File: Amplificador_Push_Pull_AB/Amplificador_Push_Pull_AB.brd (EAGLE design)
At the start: 99 x 49.8 mm, 53 parts, among them IC1 LM741P, IC3 788TV, P2 10k, Q1 BC547, Q10 TIP42C, Q2 BC547, Q4 BC547, Q7 BC547, Q8 BC547, T2 2SC1307

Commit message: Wrong positioned jumper reallocated.
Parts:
- moved IC1 0.63 mm to (61.6, 11.4)
- moved RLEFT 0.63 mm to (77.5, 7.62)
- moved RRIGHT 0.63 mm to (74.9, 7.62)
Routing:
- net GND: track 359.7 -> 388.4 mm
- net N$26: track 27.8 -> 24.4 mm
- net N$27: track 63.3 -> 60.9 mm
- net -18V: track 172.3 -> 171.1 mm
- net VIN: track 7.25 -> 6.50 mm
- net N$12: track 10.4 -> 9.79 mm
- net N$14: track 17.2 -> 16.6 mm

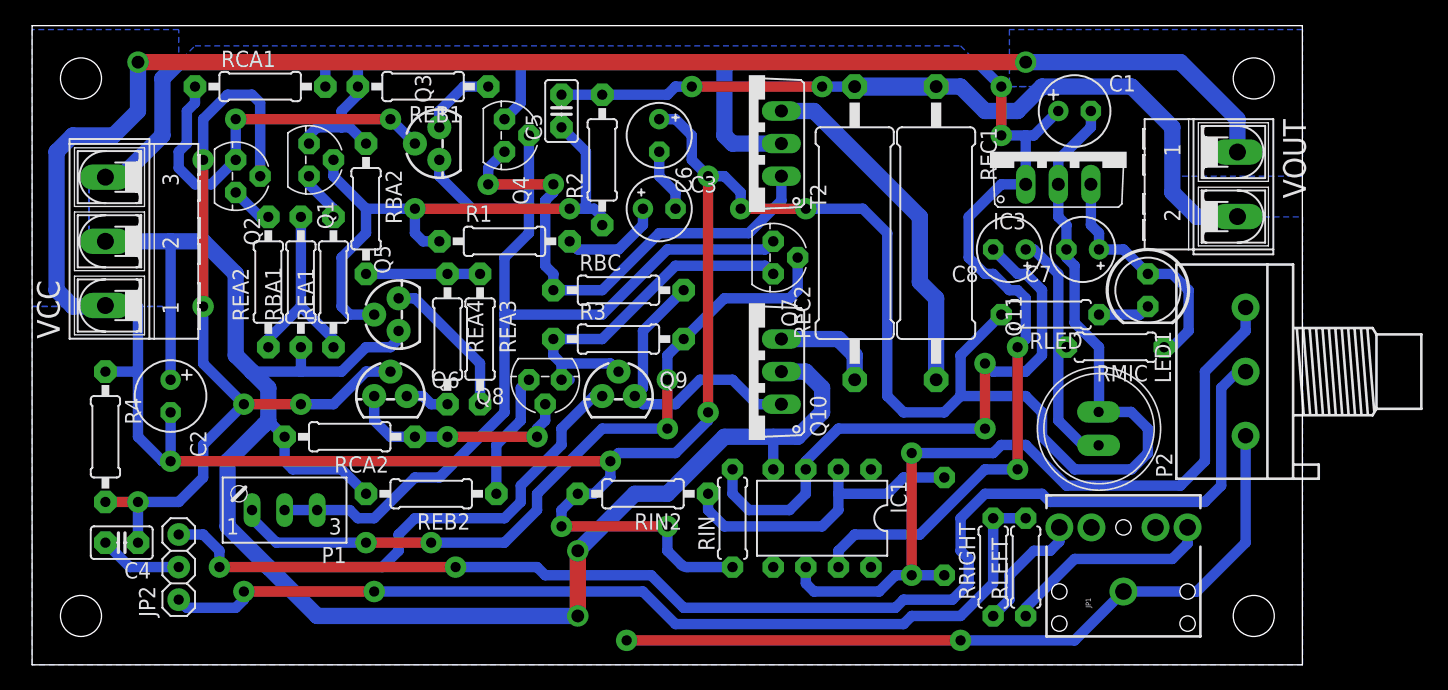
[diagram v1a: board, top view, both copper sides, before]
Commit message: Pads and vias increased outer diameter.
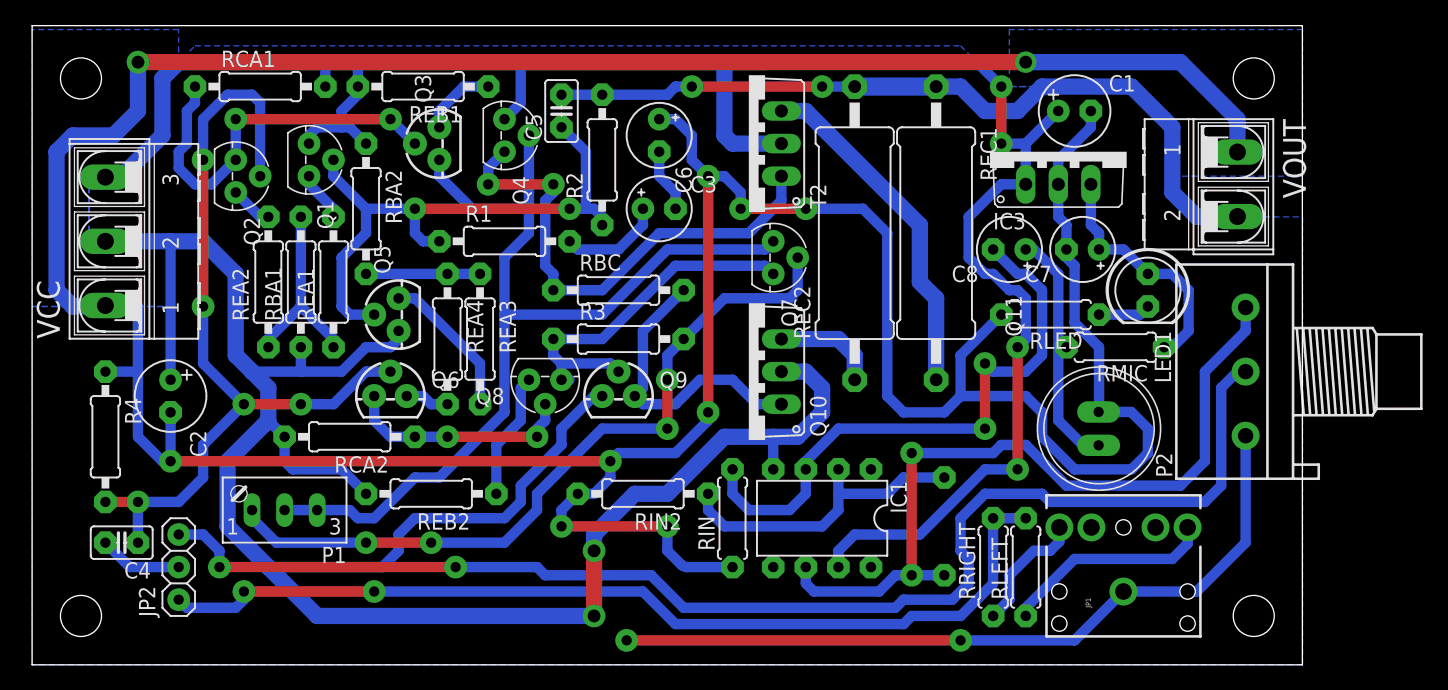
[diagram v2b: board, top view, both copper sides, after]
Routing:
- net -18V: track 171.1 -> 171.9 mm

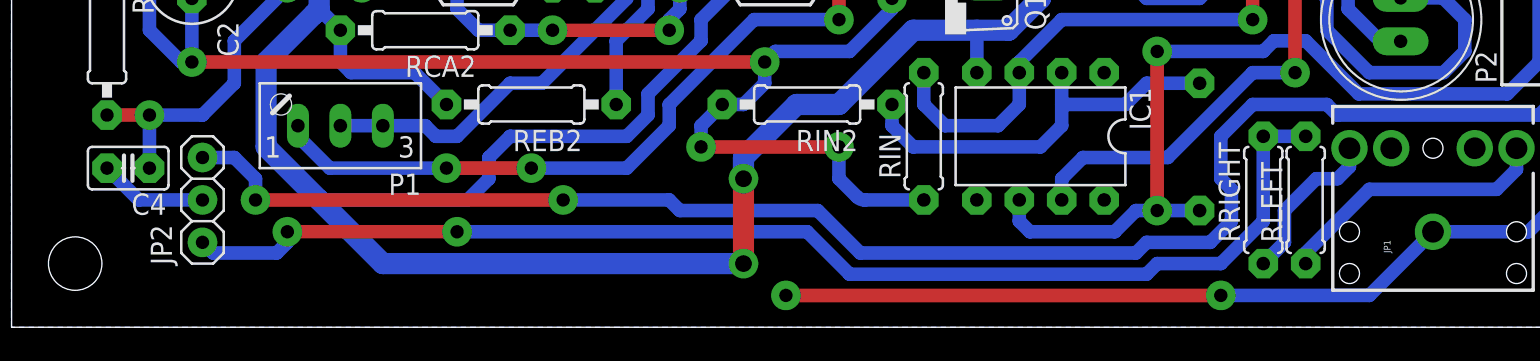
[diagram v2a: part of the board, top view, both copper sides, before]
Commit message: Double connection with jumper and resistor in one pad solved. Printable file genererated. Ready!!!
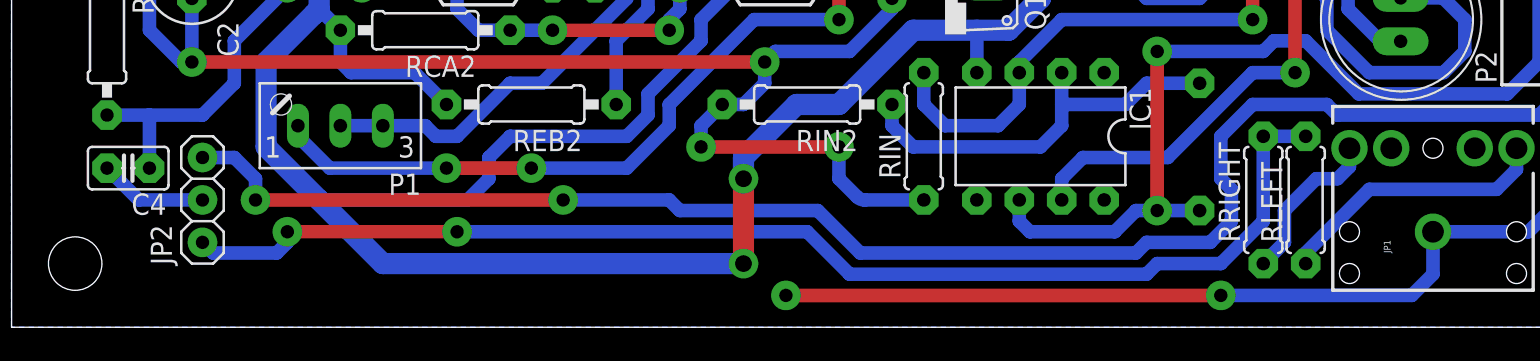
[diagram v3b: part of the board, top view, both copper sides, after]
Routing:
- net GND: track 388.4 -> 389.9 mm
- net HEHEAH: vias 5 -> 4
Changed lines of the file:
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@@
 <layer number="220" name="220bmp" color="21" fill="1" visible="no" active="no"/>
 <layer number="221" name="221bmp" color="22" fill="1" visible="no" active="no"/>
-<layer number="222" name="222bmp" color="23" fill="1" visible="no" active="no"/>
 <layer number="223" name="223bmp" color="24" fill="1" visible="no" active="no"/>
 <layer number="224" name="224bmp" color="25" fill="1" visible="no" active="no"/>
@@
 <wire x1="94.615" y1="9.525" x2="90.805" y2="5.715" width="0.8128" layer="16"/>
 <wire x1="90.805" y1="5.715" x2="85.09" y2="5.715" width="0.8128" layer="16"/>
-<wire x1="85.09" y1="5.715" x2="81.28" y2="1.905" width="0.8128" layer="16"/>
-<wire x1="81.28" y1="1.905" x2="72.39" y2="1.905" width="0.8128" layer="16"/>
+<wire x1="83.82" y1="1.905" x2="72.39" y2="1.905" width="0.8128" layer="16"/>
 <via x="72.39" y="1.905" extent="1-16" drill="0.8" diameter="1.778" shape="octagon"/>
 <wire x1="72.39" y1="1.905" x2="46.355" y2="1.905" width="0.8128" layer="1"/>
@@
 <wire x1="42.545" y1="13.335" x2="41.275" y2="12.065" width="0.8128" layer="16"/>
 <wire x1="41.275" y1="12.065" x2="41.275" y2="10.795" width="0.8128" layer="16"/>
+<wire x1="83.82" y1="1.905" x2="85.09" y2="3.175" width="0.8128" layer="16"/>
+<wire x1="85.09" y1="3.175" x2="85.09" y2="5.715" width="0.8128" layer="16"/>
 </signal>
 <signal name="N$13">
@@
 <via x="13.335" y="27.94" extent="1-16" drill="0.8" diameter="1.778" shape="octagon"/>
 <wire x1="23.495" y1="20.32" x2="26.035" y2="22.86" width="0.8128" layer="16"/>
-<wire x1="5.715" y1="12.7" x2="8.255" y2="12.7" width="0.8128" layer="1"/>
-<via x="8.255" y="12.7" extent="1-16" drill="0.8" diameter="1.778" shape="octagon"/>
 <wire x1="26.035" y1="22.86" x2="27.94" y2="22.86" width="0.8128" layer="16"/>
 <wire x1="23.495" y1="20.32" x2="20.955" y2="20.32" width="0.8128" layer="16"/>
@@
 <wire x1="15.24" y1="44.45" x2="13.335" y2="42.545" width="0.8128" layer="16"/>
 <wire x1="13.335" y1="42.545" x2="13.335" y2="39.37" width="0.8128" layer="16"/>
+<wire x1="5.715" y1="12.7" x2="8.255" y2="12.7" width="0.8128" layer="16"/>
 </signal>
 <signal name="N$18">

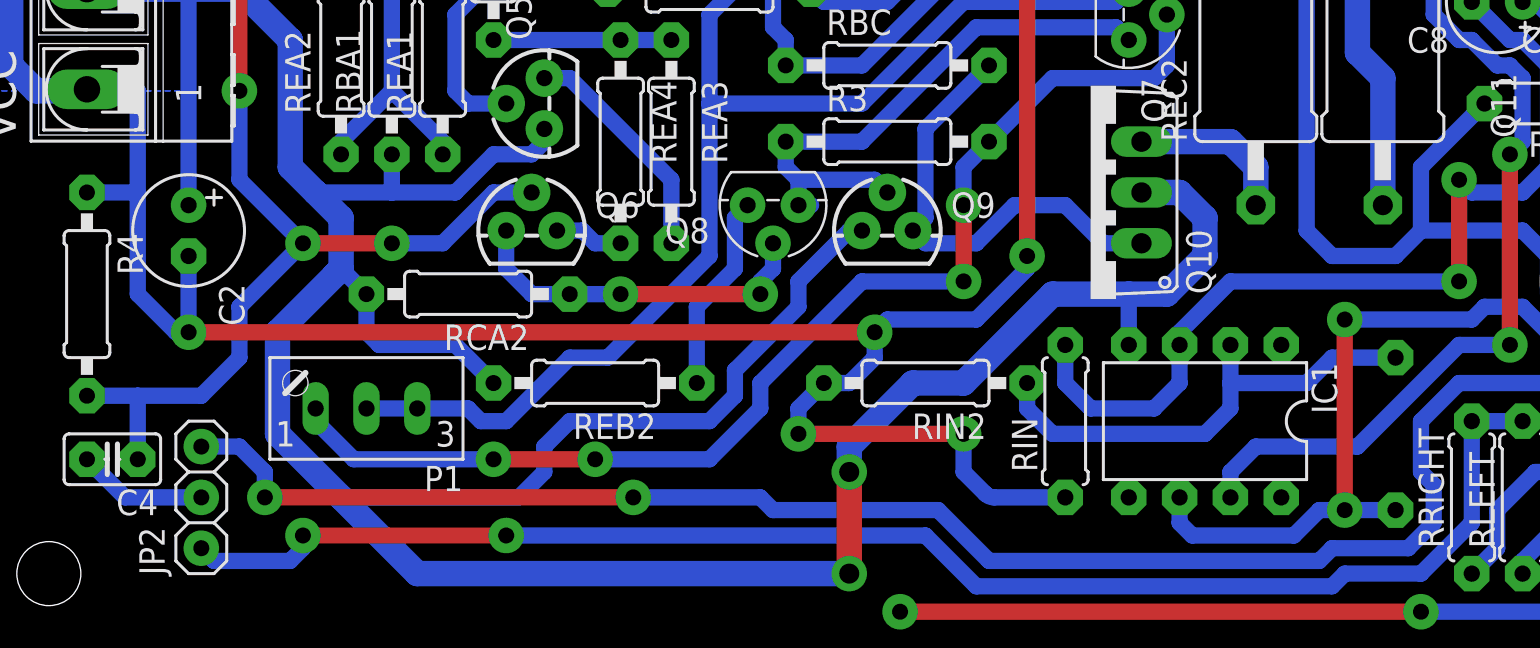
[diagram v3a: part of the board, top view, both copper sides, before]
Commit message: Inversed polarity capactitor problem solved. Simulation files added. PCB assembled and worked good! Next time: Limit the outputs's maximum voltage of the op. amp. through a smaller gain or decrease the potentiometer range; Also, swap the pin header used in channel selection for HH key bought.
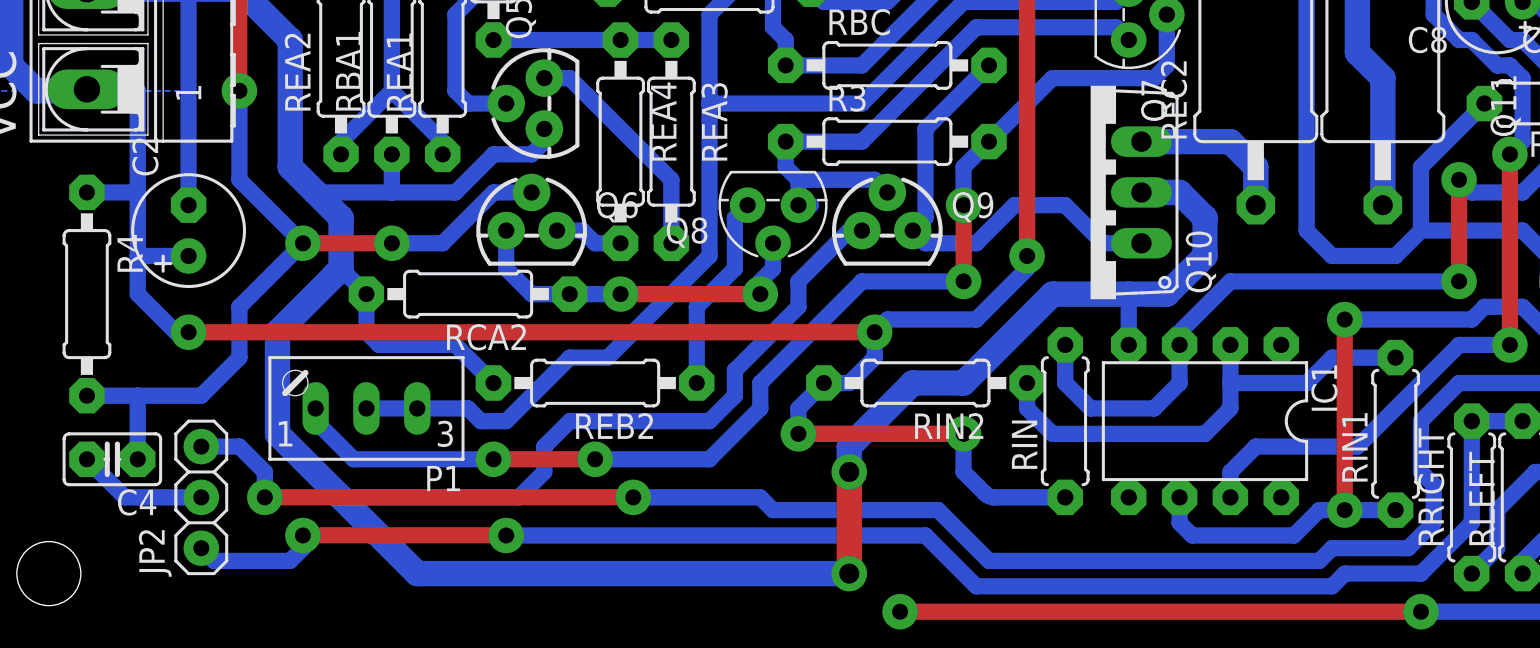
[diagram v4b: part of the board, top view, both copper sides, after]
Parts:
- C7, C8: value 0.1uF -> 0.68uF
- P2: value 10k -> 100k
- RIN1: value 100k -> 22k
- turned C2 to 90 degrees
- flipped RIN1 to the top
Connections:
- net -18V: now also C2.-; no longer C2.+
- net GND: now also C2.+; no longer C2.-
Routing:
- net GND: track 389.9 -> 388.6 mm
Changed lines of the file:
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@@
 <elements>
 <element name="C1" library="rcl" package="E2,5-6" value="100uF" x="81.28" y="43.18"/>
-<element name="C2" library="rcl" package="E2,5-6" value="100uF" x="10.795" y="20.955" rot="R270"/>
+<element name="C2" library="rcl" package="E2,5-6" value="100uF" x="10.795" y="20.955" rot="R90"/>
 <element name="C3" library="rcl" package="E2,5-5" value="10uF" x="48.895" y="35.56"/>
 <element name="Q1" library="transistor" package="TO92" value="BC547" x="21.59" y="39.37" rot="R270"/>
@@
 <element name="Q11" library="adafruit" package="9.7ELECTRET" value="" x="83.185" y="18.415" rot="R270"/>
 <element name="C6" library="rcl" package="E2,5-5" value="10uF" x="48.895" y="41.275" rot="R270"/>
-<element name="C7" library="rcl" package="E2,5-5" value="0.1uF" x="81.915" y="32.385" rot="R180"/>
-<element name="C8" library="rcl" package="E2,5-5" value="0.1uF" x="76.2" y="32.385" rot="R180"/>
+<element name="C7" library="rcl" package="E2,5-5" value="0.68uF" x="81.915" y="32.385" rot="R180"/>
+<element name="C8" library="rcl" package="E2,5-5" value="0.68uF" x="76.2" y="32.385" rot="R180"/>
 <element name="RIN" library="rcl" package="0207/7" value="100k" x="54.61" y="11.43" rot="R90"/>
-<element name="RIN1" library="rcl" package="0207/7" value="100k" x="71.12" y="10.795" rot="MR90"/>
+<element name="RIN1" library="rcl" package="0207/7" value="22k" x="71.12" y="10.795" rot="R90"/>
 <element name="RIN2" library="rcl" package="0207/10" value="10k" x="47.625" y="13.335" rot="R180"/>
-<element name="P2" library="pot" package="3RP/1610N" value="10k" x="94.615" y="22.86" rot="R90"/>
+<element name="P2" library="pot" package="3RP/1610N" value="100k" x="94.615" y="22.86" rot="R90"/>
 <element name="JP2" library="pinhead" package="1X03" value="" x="11.43" y="7.62" rot="R90"/>
 <element name="RLEFT" library="rcl" package="0207/7" value="10k" x="77.47" y="7.62" rot="R90"/>
@@
 <contactref element="R4" pad="1"/>
 <contactref element="C1" pad="-"/>
-<contactref element="C2" pad="-"/>
 <contactref element="VOUT" pad="1"/>
 <contactref element="VCC" pad="1"/>
@@
 <wire x1="5.07773125" y1="27.975521875" x2="5.1181" y2="27.9781" width="1.27" layer="16"/>
 <wire x1="5.1181" y1="27.9781" x2="5.715" y2="28.0162" width="1.27" layer="16"/>
-<wire x1="10.795" y1="19.685" x2="10.795" y2="15.875" width="0.8128" layer="16"/>
 <wire x1="5.715" y1="22.86" x2="8.255" y2="22.86" width="0.8128" layer="16"/>
 <via x="41.275" y="10.795" extent="1-16" drill="0.8" diameter="1.778" shape="octagon"/>
@@
 <wire x1="67.945" y1="19.685" x2="66.675" y2="20.955" width="0.8128" layer="16"/>
 <wire x1="66.675" y1="20.955" x2="66.675" y2="33.655" width="0.8128" layer="16"/>
-<wire x1="8.255" y1="17.78" x2="8.255" y2="22.86" width="0.8128" layer="16"/>
+<wire x1="8.255" y1="17.78" x2="8.255" y2="19.685" width="0.8128" layer="16"/>
+<wire x1="8.255" y1="19.685" x2="8.255" y2="22.86" width="0.8128" layer="16"/>
 <wire x1="8.255" y1="22.86" x2="8.255" y2="27.94" width="0.8128" layer="16"/>
 <wire x1="45.085" y1="14.605" x2="43.815" y2="13.335" width="0.8128" layer="16"/>
@@
 <wire x1="83.82" y1="1.905" x2="85.09" y2="3.175" width="0.8128" layer="16"/>
 <wire x1="85.09" y1="3.175" x2="85.09" y2="5.715" width="0.8128" layer="16"/>
+<contactref element="C2" pad="+"/>
+<wire x1="10.795" y1="19.685" x2="8.255" y2="19.685" width="0.8128" layer="16"/>
 </signal>
 <signal name="N$13">
@@
 <contactref element="REB2" pad="2"/>
 <contactref element="Q10" pad="C"/>
-<contactref element="C2" pad="+"/>
 <contactref element="RBA1" pad="1"/>
 <contactref element="Q9" pad="1"/>
 <contactref element="VCC" pad="2"/>
 <wire x1="13.335" y1="33.02" x2="15.875" y2="30.48" width="1.27" layer="16"/>
-<wire x1="13.335" y1="33.02" x2="10.795" y2="33.02" width="1.27" layer="16"/>
 <wire x1="20.955" y1="24.765" x2="20.955" y2="22.86" width="0.8128" layer="16"/>
 <wire x1="26.035" y1="24.765" x2="24.13" y2="22.86" width="0.8128" layer="16"/>
 <wire x1="24.13" y1="22.86" x2="20.955" y2="22.86" width="0.8128" layer="16"/>
 <contactref element="IC1" pad="4"/>
-<wire x1="10.795" y1="22.225" x2="10.795" y2="33.02" width="0.8128" layer="16"/>
 <via x="43.815" y="8.89" extent="1-16" drill="1" diameter="1.778" shape="octagon"/>
 <wire x1="43.815" y1="8.89" x2="43.815" y2="3.81" width="1.27" layer="1"/>
@@
 <wire x1="38.1" y1="13.97" x2="38.1" y2="12.7" width="0.8128" layer="16"/>
 <wire x1="38.1" y1="12.7" x2="36.83" y2="11.43" width="0.8128" layer="16"/>
+<wire x1="13.335" y1="33.02" x2="10.795" y2="33.02" width="1.27" layer="16"/>
 <wire x1="10.795" y1="33.02" x2="5.715" y2="33.02" width="1.27" layer="16"/>
 <wire x1="36.83" y1="11.43" x2="29.845" y2="11.43" width="0.8128" layer="16"/>
@@
 <wire x1="43.815" y1="8.89" x2="43.815" y2="10.16" width="1.27" layer="16"/>
 <wire x1="43.815" y1="10.16" x2="46.99" y2="13.335" width="1.27" layer="16"/>
+<contactref element="C2" pad="-"/>
+<wire x1="10.795" y1="22.225" x2="10.795" y2="33.02" width="0.8128" layer="16"/>
 </signal>
 <signal name="N$23">
@@
 <contactref element="IC1" pad="2"/>
 <contactref element="RIN2" pad="1"/>
-<wire x1="67.945" y1="14.605" x2="71.12" y2="14.605" width="0.8128" layer="16"/>
 <wire x1="52.705" y1="12.065" x2="52.705" y2="13.335" width="0.8128" layer="16"/>
-<wire x1="67.945" y1="14.605" x2="66.675" y2="13.335" width="0.8128" layer="16"/>
 <wire x1="66.675" y1="13.335" x2="62.865" y2="13.335" width="0.8128" layer="16"/>
 <wire x1="62.865" y1="13.335" x2="62.865" y2="15.24" width="0.8128" layer="16"/>
@@
 <wire x1="61.595" y1="10.795" x2="53.975" y2="10.795" width="0.8128" layer="16"/>
 <wire x1="53.975" y1="10.795" x2="52.705" y2="12.065" width="0.8128" layer="16"/>
+<wire x1="66.675" y1="13.335" x2="67.945" y2="14.605" width="0.8128" layer="16"/>
+<wire x1="67.945" y1="14.605" x2="71.12" y2="14.605" width="0.8128" layer="16"/>
 </signal>
 <signal name="N$27">
@@
 <wire x1="91.44" y1="22.86" x2="94.615" y2="26.035" width="0.8128" layer="16"/>
 <wire x1="94.615" y1="26.035" x2="94.615" y2="27.86" width="0.8128" layer="16"/>
-<wire x1="71.12" y1="6.985" x2="68.58" y2="6.985" width="0.8128" layer="16"/>
 <wire x1="68.58" y1="6.985" x2="67.31" y2="6.985" width="0.8128" layer="16"/>
 <wire x1="67.31" y1="6.985" x2="66.04" y2="5.715" width="0.8128" layer="16"/>
@@
 <wire x1="75.565" y1="17.145" x2="77.47" y2="17.145" width="0.8128" layer="16"/>
 <wire x1="77.47" y1="17.145" x2="80.645" y2="13.97" width="0.8128" layer="16"/>
+<wire x1="71.12" y1="6.985" x2="68.58" y2="6.985" width="0.8128" layer="16"/>
 </signal>
 <signal name="N$30">
